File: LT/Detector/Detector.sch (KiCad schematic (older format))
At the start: 10 parts, among them J1 Conn_01x02_Male, J2 Conn_Coaxial, J3 Conn_Coaxial, J4 Conn_01x02_Male, U1 AD8361

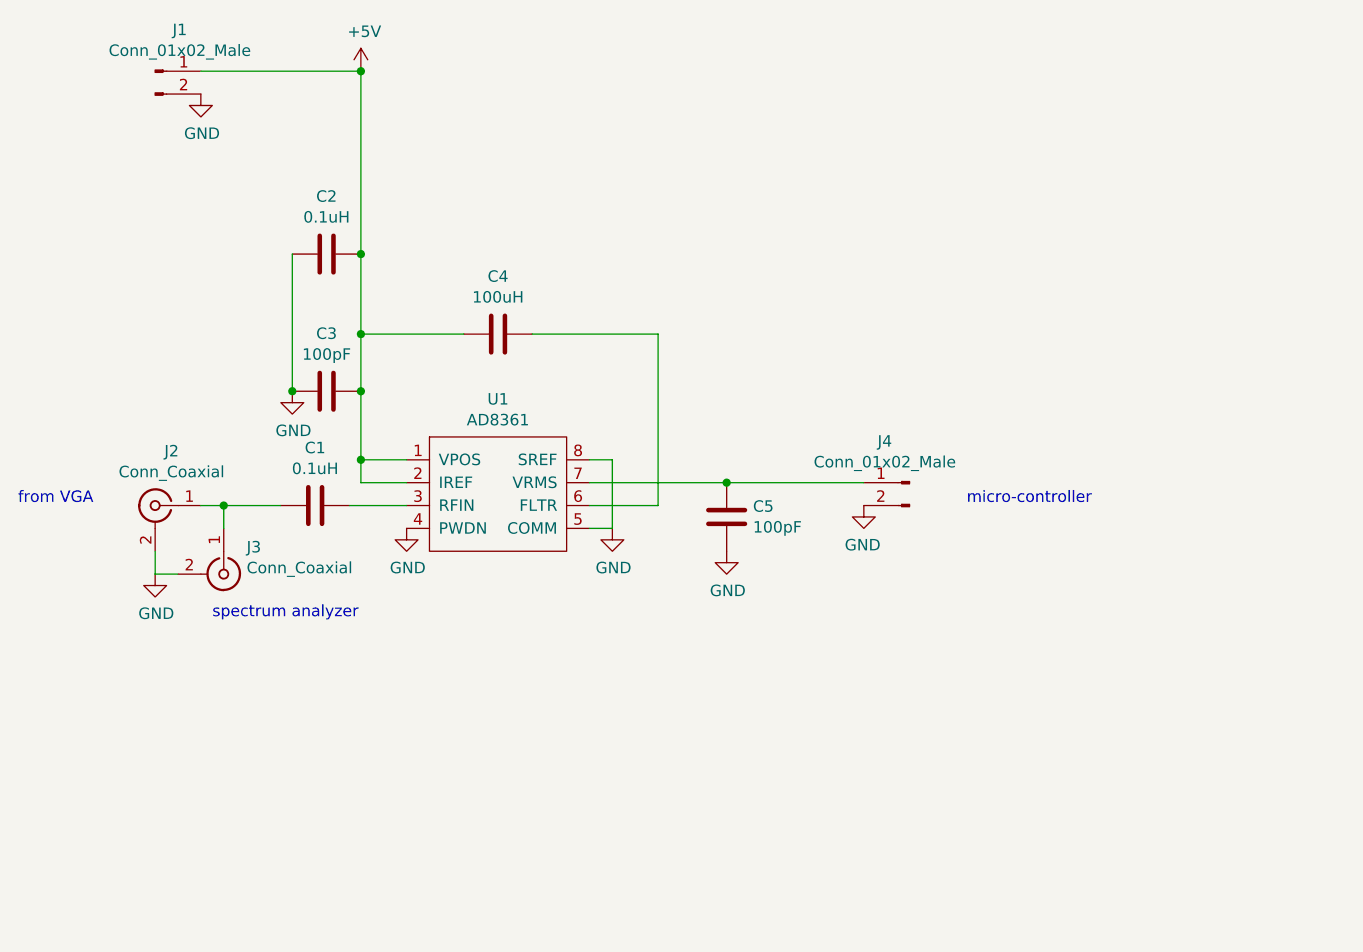
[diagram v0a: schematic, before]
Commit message: Uploaded Schematics to Integration of Phase 2
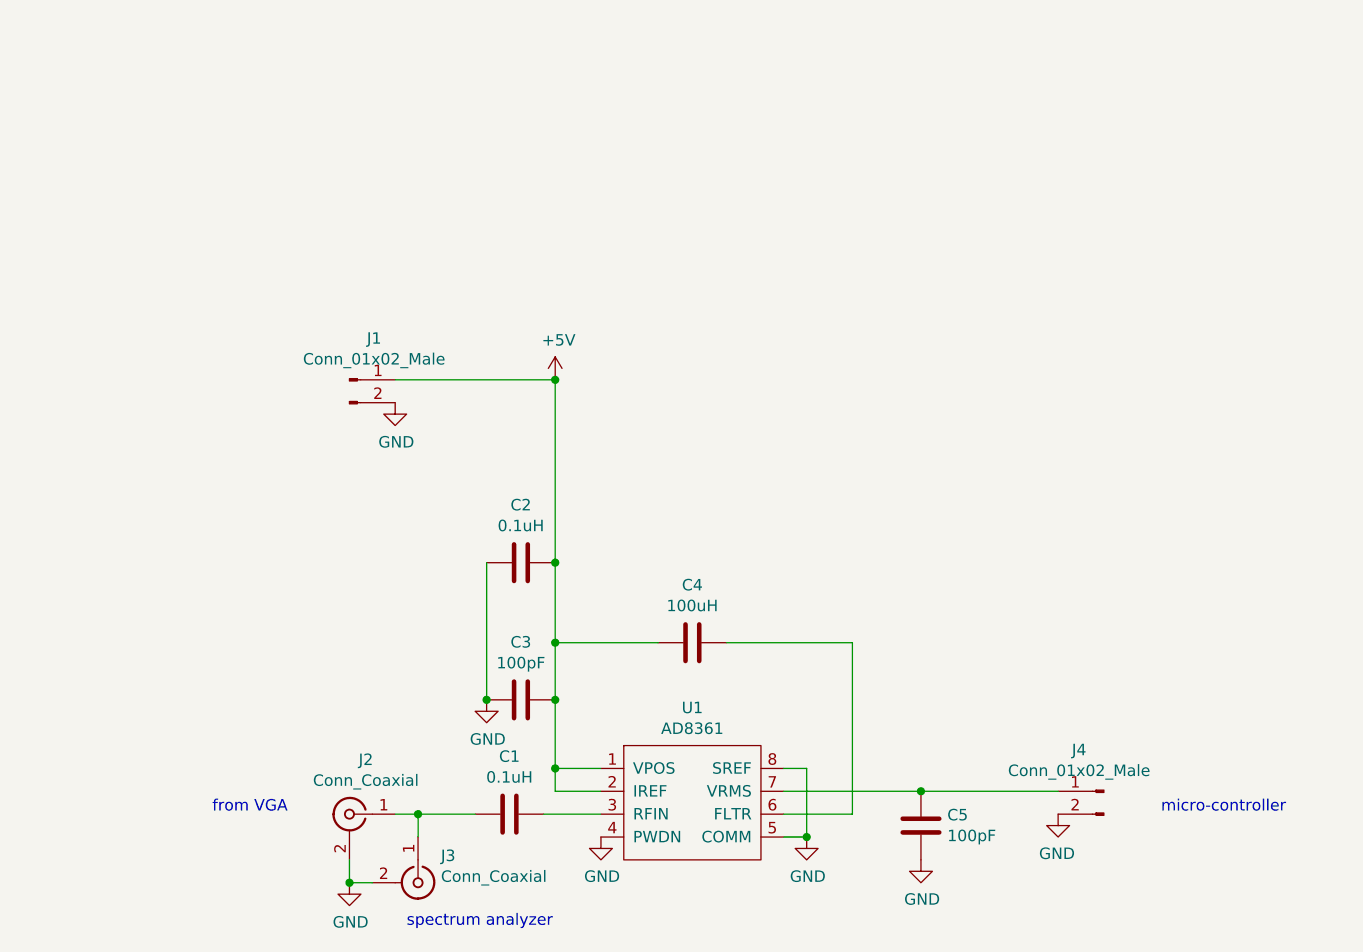
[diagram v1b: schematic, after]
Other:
- moved on the sheet: C1, C2, C3, C4, C5, J1, J2, J3, J4, U1
